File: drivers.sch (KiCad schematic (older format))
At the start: 27 parts, among them U1 K, U2 E, U3 F

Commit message: - added supply sch draft
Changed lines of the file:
@@
 $Descr A4 11693 8268
 encoding utf-8
-Sheet 9 8
+Sheet 8 9
 Title ""
 Date ""
@@
 $EndComp
 $Comp
-L power:GND #PWR?
-U 1 1 5F61F5A5
-P 5200 2000
-F 0 "#PWR?" H 5200 1840 50  0001 C CNN
-F 1 "GND" V 5200 1923 39  0000 R CNN
-F 2 "" H 5200 2000 50  0001 C CNN
-F 3 "" H 5200 2000 50  0001 C CNN
-	1    5200 2000
-	1    0    0    -1
-$EndComp
-$Comp
 L power:+12V #PWR?
 U 1 1 5F61F5AB
@@
 Wire Wire Line
 	5200 2000 5200 1850
-Connection ~ 5200 2000
 Wire Wire Line
 	4950 1700 4600 1700
@@
 $EndComp
 $Comp
-L power:GND #PWR?
-U 1 1 5F61F5ED
-P 6450 1650
-F 0 "#PWR?" H 6450 1490 50  0001 C CNN
-F 1 "GND" V 6450 1573 39  0000 R CNN
-F 2 "" H 6450 1650 50  0001 C CNN
-F 3 "" H 6450 1650 50  0001 C CNN
-	1    6450 1650
-	1    0    0    -1
-$EndComp
-$Comp
 L power:+15V #PWR?
 U 1 1 5F61F5F3
@@
 	4600 1700 4000 1700
 $Comp
-L power:GND #PWR?
-U 1 1 5F620EBC
-P 5200 3600
-F 0 "#PWR?" H 5200 3440 50  0001 C CNN
-F 1 "GND" V 5200 3523 39  0000 R CNN
-F 2 "" H 5200 3600 50  0001 C CNN
-F 3 "" H 5200 3600 50  0001 C CNN
-	1    5200 3600
-	1    0    0    -1
-$EndComp
-$Comp
 L power:+12V #PWR?
 U 1 1 5F620EC2
@@
 Wire Wire Line
 	5200 3600 5200 3450
-Connection ~ 5200 3600
 Wire Wire Line
 	4950 3300 4600 3300
@@
 	4600 3300 4000 3300
 $Comp
-L power:GND #PWR?
-U 1 1 5F62129D
-P 5200 5200
-F 0 "#PWR?" H 5200 5040 50  0001 C CNN
-F 1 "GND" V 5200 5123 39  0000 R CNN
-F 2 "" H 5200 5200 50  0001 C CNN
-F 3 "" H 5200 5200 50  0001 C CNN
-	1    5200 5200
-	1    0    0    -1
-$EndComp
-$Comp
 L power:+12V #PWR?
 U 1 1 5F6212A3
@@
 Wire Wire Line
 	5200 5200 5200 5050
-Connection ~ 5200 5200
 Wire Wire Line
 	4950 4900 4600 4900
@@
 $EndComp
 $Comp
-L power:GND #PWR?
-U 1 1 5F622691
-P 6450 3300
-F 0 "#PWR?" H 6450 3140 50  0001 C CNN
-F 1 "GND" V 6450 3223 39  0000 R CNN
-F 2 "" H 6450 3300 50  0001 C CNN
-F 3 "" H 6450 3300 50  0001 C CNN
-	1    6450 3300
-	1    0    0    -1
-$EndComp
-$Comp
 L power:+15V #PWR?
 U 1 1 5F622697
@@
 $EndComp
 $Comp
-L power:GND #PWR?
-U 1 1 5F622A77
-P 6450 4950
-F 0 "#PWR?" H 6450 4790 50  0001 C CNN
-F 1 "GND" V 6450 4873 39  0000 R CNN
-F 2 "" H 6450 4950 50  0001 C CNN
-F 3 "" H 6450 4950 50  0001 C CNN
-	1    6450 4950
-	1    0    0    -1
-$EndComp
-$Comp
 L power:+15V #PWR?
 U 1 1 5F622A7D
@@
 	1    0    0    -1
 $EndComp
+$Comp
+L power:GND #PWR?
+U 1 1 5F62755D
+P 6450 1650
+AR Path="/5F40DCB9/5F62755D" Ref="#PWR?"  Part="1"
+AR Path="/5F618AB9/5F62755D" Ref="#PWR?"  Part="1"
+AR Path="/5F62755D" Ref="#PWR?"  Part="1"
+AR Path="/5F61C123/5F62755D" Ref="#PWR?"  Part="1"
+F 0 "#PWR?" H 6450 1490 50  0001 C CNN
+F 1 "GND" H 6450 1550 39  0000 C TNN
+F 2 "" H 6450 1650 50  0001 C CNN
+F 3 "" H 6450 1650 50  0001 C CNN
+	1    6450 1650
+	1    0    0    -1
+$EndComp
+$Comp
+L power:GND #PWR?
+U 1 1 5F6278F0
+P 5200 2000
+AR Path="/5F40DCB9/5F6278F0" Ref="#PWR?"  Part="1"
+AR Path="/5F618AB9/5F6278F0" Ref="#PWR?"  Part="1"
+AR Path="/5F6278F0" Ref="#PWR?"  Part="1"
+AR Path="/5F61C123/5F6278F0" Ref="#PWR?"  Part="1"
+F 0 "#PWR?" H 5200 1840 50  0001 C CNN
+F 1 "GND" H 5200 1900 39  0000 C TNN
+F 2 "" H 5200 2000 50  0001 C CNN
+F 3 "" H 5200 2000 50  0001 C CNN
+	1    5200 2000
+	1    0    0    -1
+$EndComp
+$Comp
+L power:GND #PWR?
+U 1 1 5F627D40
+P 6450 3300
+AR Path="/5F40DCB9/5F627D40" Ref="#PWR?"  Part="1"
+AR Path="/5F618AB9/5F627D40" Ref="#PWR?"  Part="1"
+AR Path="/5F627D40" Ref="#PWR?"  Part="1"
+AR Path="/5F61C123/5F627D40" Ref="#PWR?"  Part="1"
+F 0 "#PWR?" H 6450 3140 50  0001 C CNN
+F 1 "GND" H 6450 3200 39  0000 C TNN
+F 2 "" H 6450 3300 50  0001 C CNN
+F 3 "" H 6450 3300 50  0001 C CNN
+	1    6450 3300
+	1    0    0    -1
+$EndComp
+$Comp
+L power:GND #PWR?
+U 1 1 5F6280D3
+P 5200 3600
+AR Path="/5F40DCB9/5F6280D3" Ref="#PWR?"  Part="1"
+AR Path="/5F618AB9/5F6280D3" Ref="#PWR?"  Part="1"
+AR Path="/5F6280D3" Ref="#PWR?"  Part="1"
+AR Path="/5F61C123/5F6280D3" Ref="#PWR?"  Part="1"
+F 0 "#PWR?" H 5200 3440 50  0001 C CNN
+F 1 "GND" H 5200 3500 39  0000 C TNN
+F 2 "" H 5200 3600 50  0001 C CNN
+F 3 "" H 5200 3600 50  0001 C CNN
+	1    5200 3600
+	1    0    0    -1
+$EndComp
+$Comp
+L power:GND #PWR?
+U 1 1 5F628523
+P 6450 4950
+AR Path="/5F40DCB9/5F628523" Ref="#PWR?"  Part="1"
+AR Path="/5F618AB9/5F628523" Ref="#PWR?"  Part="1"
+AR Path="/5F628523" Ref="#PWR?"  Part="1"
+AR Path="/5F61C123/5F628523" Ref="#PWR?"  Part="1"
+F 0 "#PWR?" H 6450 4790 50  0001 C CNN
+F 1 "GND" H 6450 4850 39  0000 C TNN
+F 2 "" H 6450 4950 50  0001 C CNN
+F 3 "" H 6450 4950 50  0001 C CNN
+	1    6450 4950
+	1    0    0    -1
+$EndComp
+$Comp
+L power:GND #PWR?
+U 1 1 5F6288B6
+P 5200 5200
+AR Path="/5F40DCB9/5F6288B6" Ref="#PWR?"  Part="1"
+AR Path="/5F618AB9/5F6288B6" Ref="#PWR?"  Part="1"
+AR Path="/5F6288B6" Ref="#PWR?"  Part="1"
+AR Path="/5F61C123/5F6288B6" Ref="#PWR?"  Part="1"
+F 0 "#PWR?" H 5200 5040 50  0001 C CNN
+F 1 "GND" H 5200 5100 39  0000 C TNN
+F 2 "" H 5200 5200 50  0001 C CNN
+F 3 "" H 5200 5200 50  0001 C CNN
+	1    5200 5200
+	1    0    0    -1
+$EndComp
+Connection ~ 5200 5200
+Connection ~ 5200 3600
+Connection ~ 5200 2000
 $EndSCHEMATC

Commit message: - added footprint & 3D model of DC/DC HV converter - updated battery (to 2x battery holder) - some changes in supply
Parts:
- U1, U2, U3: footprint (none) -> Library_uScope:APD_P2_single
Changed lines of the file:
@@
 $Descr A4 11693 8268
 encoding utf-8
-Sheet 8 9
+Sheet 6 9
 Title ""
 Date ""
@@
 F 0 "U1" H 5728 1751 50  0000 L CNN
 F 1 "K" H 5728 1660 50  0000 L CNN
-F 2 "" H 5500 1700 50  0001 C CNN
+F 2 "Library_uScope:APD_P2_single" H 5500 1700 50  0001 C CNN
 F 3 "" H 5500 1700 50  0001 C CNN
 	1    5500 1700
@@
 F 0 "U2" H 5728 3351 50  0000 L CNN
 F 1 "E" H 5728 3260 50  0000 L CNN
-F 2 "" H 5500 3300 50  0001 C CNN
+F 2 "Library_uScope:APD_P2_single" H 5500 3300 50  0001 C CNN
 F 3 "" H 5500 3300 50  0001 C CNN
 	1    5500 3300
@@
 F 0 "U3" H 5728 4951 50  0000 L CNN
 F 1 "F" H 5728 4860 50  0000 L CNN
-F 2 "" H 5500 4900 50  0001 C CNN
+F 2 "Library_uScope:APD_P2_single" H 5500 4900 50  0001 C CNN
 F 3 "" H 5500 4900 50  0001 C CNN
 	1    5500 4900

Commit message: - W.i.P.
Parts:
- removed C? (x2): 1n, symbol Device:C_Small
- removed Q? (x2): NMOS, symbol Device:Q_NMOS_GDS
- removed R? (x2): 10k, symbol Device:R
- removed R? (x2): 1k, symbol Device:R
- removed R? (x2): 12k, symbol Device:R
- removed R? (x2): 4k3, symbol Device:R
- removed U? (x6): LMC6482, symbol Amplifier_Operational:LMC6482
- added C? (x3): 100n, Capacitor_SMD:C_0805_2012Metric_Pad1.15x1.40mm_HandSolder, symbol Device:C_Small
- added C? (x2): 100p, Capacitor_SMD:C_0805_2012Metric_Pad1.15x1.40mm_HandSolder, symbol Device:C_Small
- added Q? (x2): BUK98150-55A, Package_TO_SOT_SMD:SOT-223-3_TabPin2, symbol Device:Q_NMOS_GDS
- added R? (x2): 10k, Resistor_SMD:R_0603_1608Metric_Pad1.05x0.95mm_HandSolder, symbol Device:R_Small
- added R? (x2): 1k, Resistor_SMD:R_0603_1608Metric_Pad1.05x0.95mm_HandSolder, symbol Device:R_Small
- added R? (x2): 12k, Resistor_SMD:R_0603_1608Metric_Pad1.05x0.95mm_HandSolder, symbol Device:R_Small
- added R? (x2): 4k3, Resistor_SMD:R_0603_1608Metric_Pad1.05x0.95mm_HandSolder, symbol Device:R_Small
- added U? (x3): LM321, Package_TO_SOT_SMD:SOT-23-5, symbol Amplifier_Operational:LM321
- C?: value 1n -> 100p; footprint (none) -> Capacitor_SMD:C_0805_2012Metric_Pad1.15x1.40mm_HandSolder
- Q?: value NMOS -> BUK98150-55A; footprint (none) -> Package_TO_SOT_SMD:SOT-223-3_TabPin2; Mfr. (none) -> Nexperia; Price [PLN] (none) -> 1.60
- R? (x4): footprint (none) -> Resistor_SMD:R_0603_1608Metric_Pad1.05x0.95mm_HandSolder; symbol Device:R -> Device:R_Small
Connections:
- net +12V: now also Q?.2 (D), Q?.2 (D)
- net +15V: now also C?.2, C?.2, C?.2, U?.5 (V+), U?.5 (V+), U?.5 (V+)
- net GND: now also C?.1, C?.1, C?.1, R?.2, R?.2, U?.2 (V-), U?.2 (V-), U?.2 (V-)
- net dac_E: now also R?.1
- net dac_F: now also R?.1
- net at U2.1 (in+): now also Q?.3 (S), R?.1
- net at U3.1 (in+): now also Q?.3 (S), R?.1
- net at C?.1, R?.1: now also U?.4
- net at C?.2, R?.1, R?.2: now also U?.3 (-)
- net at R?.2: now also U?.1 (+)
- new net: R?.2, U?.1 (+) (x2)
- new net: C?.1, R?.1, U?.4 (x2)
- new net: Q?.1 (G), R?.2 (x2)
- new net: C?.2, R?.1, R?.2, U?.3 (-) (x2)
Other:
- moved on the sheet: C?, Q?, R?, U1A, U2A, U3A

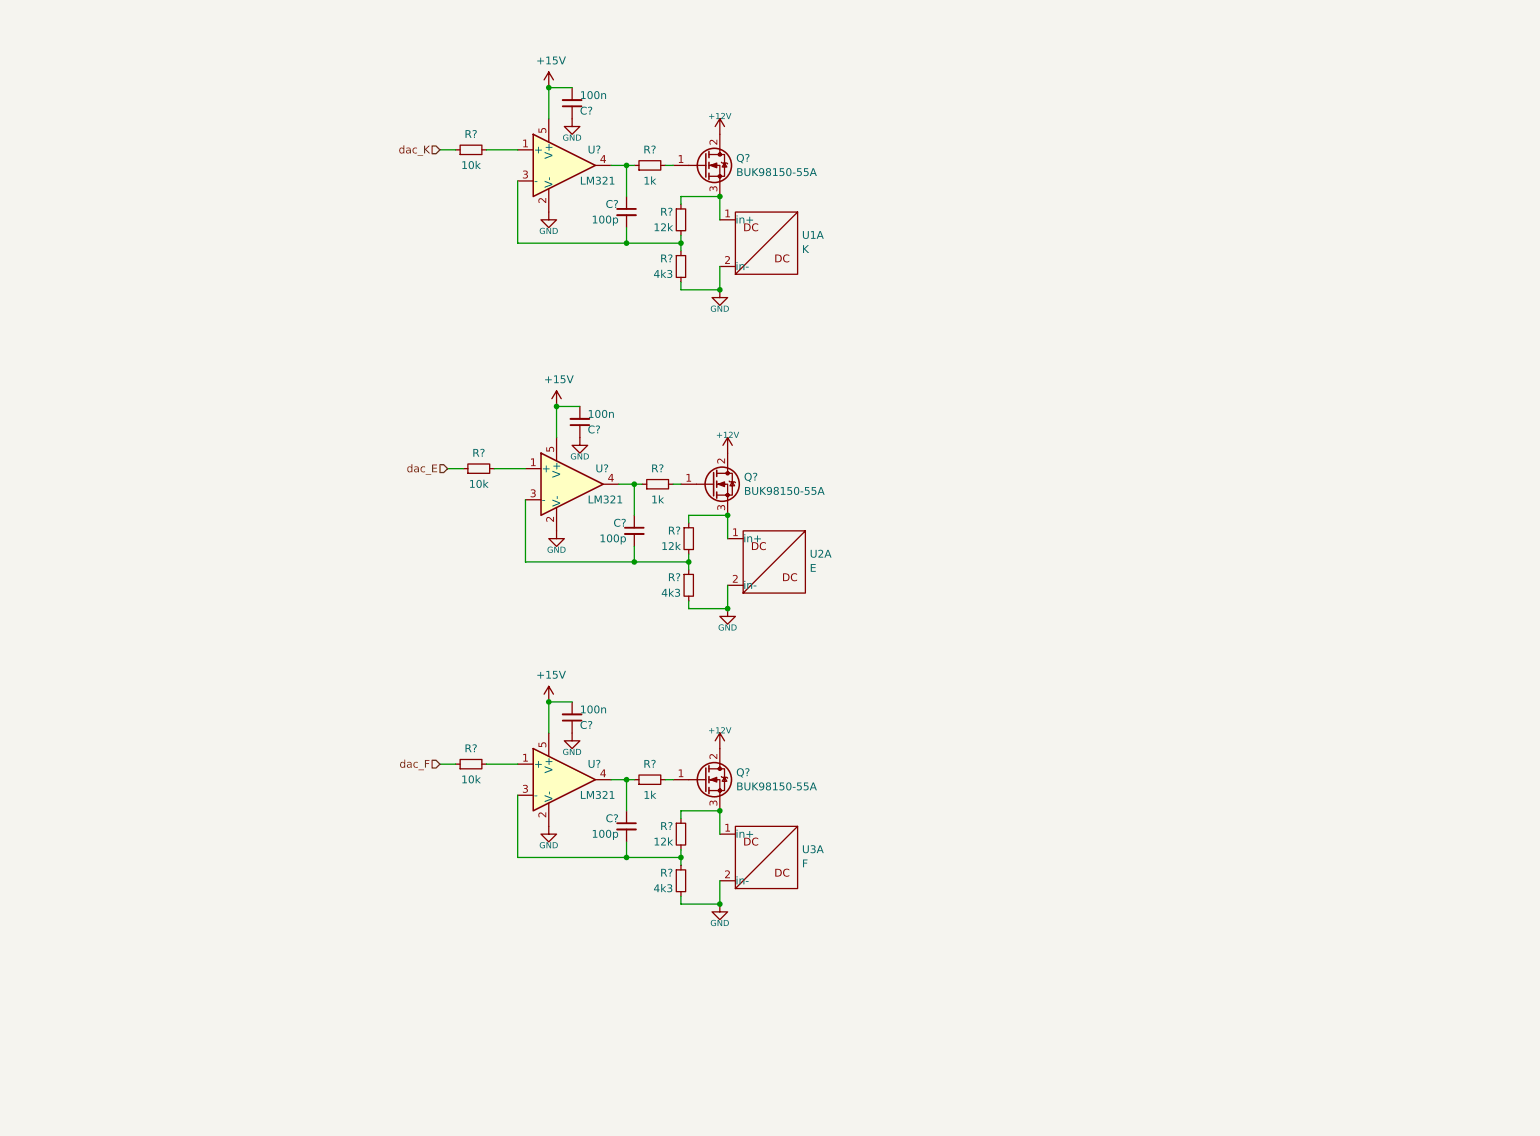
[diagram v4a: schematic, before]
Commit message: - drivers modified - MCU replaced
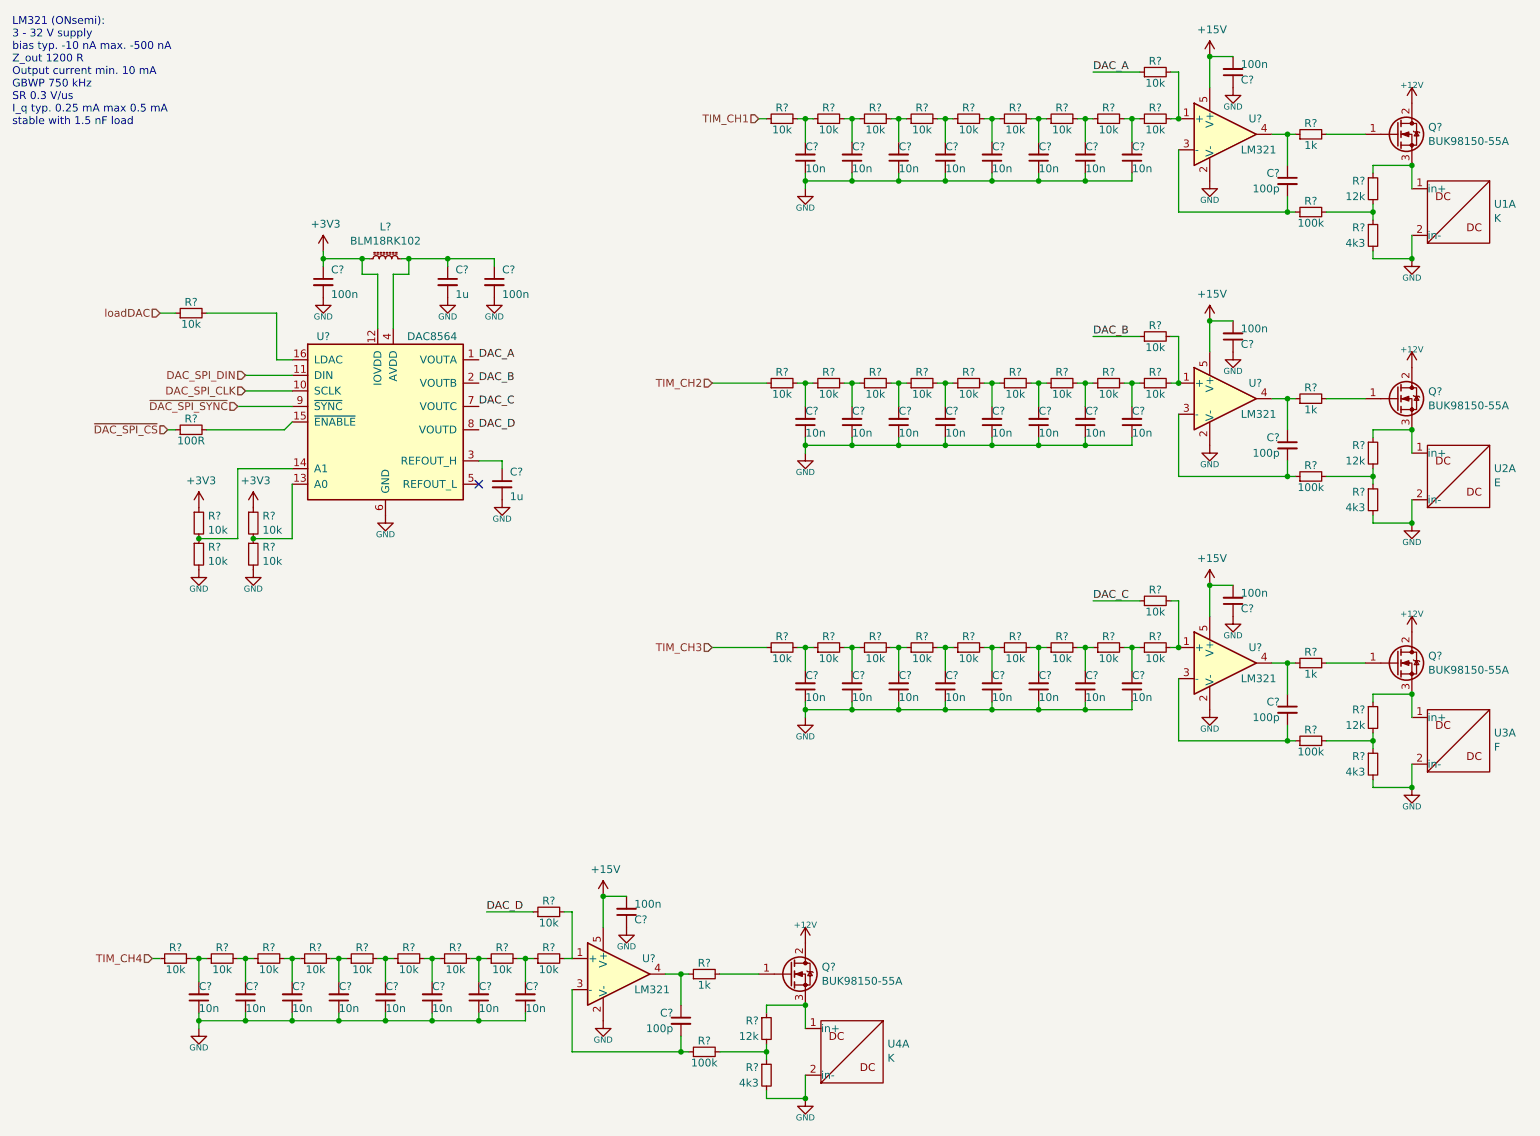
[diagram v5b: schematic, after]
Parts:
- removed R? (x3): 10k, Resistor_SMD:R_0603_1608Metric_Pad1.05x0.95mm_HandSolder, symbol Device:R_Small
- removed R? (x2): 1k, Resistor_SMD:R_0603_1608Metric_Pad1.05x0.95mm_HandSolder, symbol Device:R_Small
- added C? (x32): 10n, Capacitor_SMD:C_0603_1608Metric_Pad1.05x0.95mm_HandSolder, symbol Device:C_Small
- added C?: 100p, Capacitor_SMD:C_0805_2012Metric_Pad1.15x1.40mm_HandSolder, symbol Device:C_Small
- added C?: 100n, Capacitor_SMD:C_0805_2012Metric_Pad1.15x1.40mm_HandSolder, symbol Device:C_Small
- added C? (x2): 100n, Capacitor_SMD:C_0603_1608Metric_Pad1.05x0.95mm_HandSolder, symbol Device:C_Small
- added C? (x2): 1u, Capacitor_SMD:C_0603_1608Metric_Pad1.05x0.95mm_HandSolder, symbol Device:C_Small
- added L?: BLM18RK102, symbol Device:L_Core_Ferrite_Small
- added Q?: BUK98150-55A, Package_TO_SOT_SMD:SOT-223-3_TabPin2, symbol Device:Q_NMOS_GDS
- added R?: 12k, Resistor_SMD:R_0603_1608Metric_Pad1.05x0.95mm_HandSolder, symbol Device:R_Small
- added R?: 4k3, Resistor_SMD:R_0603_1608Metric_Pad1.05x0.95mm_HandSolder, symbol Device:R_Small
- added R? (x45): 10k, Resistor_SMD:R_0603_1608Metric_Pad1.05x0.95mm_HandSolder, symbol Device:R_Small
- added R? (x4): 100k, Resistor_SMD:R_0603_1608Metric_Pad1.05x0.95mm_HandSolder, symbol Device:R_Small
- added R? (x3): 1k, Resistor_SMD:R_0603_1608Metric_Pad1.05x0.95mm_HandSolder, symbol Device:R_Small
- added R?: 100R, Resistor_SMD:R_0603_1608Metric_Pad1.05x0.95mm_HandSolder, symbol Device:R_Small
- added U4: K, Library_uScope:APD_P2_single, symbol uScope:APD_P2_single
- added U?: LM321, Package_TO_SOT_SMD:SOT-23-5, symbol Amplifier_Operational:LM321
- added U?: DAC8564, symbol miscellaneous:DAC8564
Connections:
- net +12V: now also Q?.2 (D)
- net +15V: now also C?.2, U?.5 (V+)
- net GND: now also C?.1, C?.1, C?.1, C?.1, C?.1, C?.1, C?.1, C?.1, C?.1, C?.1, C?.1, C?.1, C?.1, C?.1, C?.1, C?.1, C?.1, C?.1, C?.1, C?.1, C?.1, C?.1, C?.1, C?.1, C?.1, C?.1, C?.1, C?.1, C?.1, C?.1, C?.1, C?.1, C?.1, C?.2, C?.2, C?.2, C?.2, R?.2, R?.2, R?.2, U4.2 (in-), U?.2 (V-), U?.6 (GND)
- net at U?.1 (+): now also R?.2, R?.2 (x3)
- net at R?.1, R?.2: now also R?.2; no longer C?.2, U?.3 (-) (x3)
- net at C?.1, U?.4: now also R?.1 (x2)
- net at Q?.1 (G): now also R?.2 (x2)
- new net: C?.2, R?.1, U?.3 (-) (x4)
- new net: C?.2, R?.1, R?.2 (x32)
- new net: Q?.3 (S), R?.1, U4.1 (in+)
- new net: R?.1, R?.2, R?.2
- new net: Q?.1 (G), R?.2
- new net: C?.1, R?.1, U?.4
- new net: R?.2, R?.2, U?.1 (+)
- new net: R?.1, R?.2, U?.14 (A1)
- new net: R?.1, R?.2, U?.13 (A0)
- new net: R?.2, U?.15 (~ENABLE)
- new net: R?.2, U?.16 (LDAC)
- new net: C?.1, U?.3 (REFOUT_H)
- new net: C?.1, C?.1, L?.2, U?.4 (AVDD)
- new net +3V3: C?.1, L?.1, R?.1, R?.1, U?.12 (IOVDD)
- new net DAC_A: R?.1, U?.1 (VOUTA)
- new net DAC_B: R?.1, U?.2 (VOUTB)
- new net DAC_C: R?.1, U?.7 (VOUTC)
- new net DAC_D: R?.1, U?.8 (VOUTD)
- new net DAC_SPI_CLK: U?.10 (SCLK)
- new net DAC_SPI_DIN: U?.11 (DIN)
- new net TIM_CH1: R?.1
- new net TIM_CH2: R?.1
- new net TIM_CH3: R?.1
- new net TIM_CH4: R?.1
- new net loadDAC: R?.1
- new net ~DAC_SPI_CS: R?.1
- new net ~DAC_SPI_SYNC: U?.9 (~SYNC)
- no-connect marks 0 -> 1
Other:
- note added: "LM321 (ONsemi):\n3 - 32 V supply\nbias typ. -10 nA max. -500 nA\nZ_out 1200 R\nOutput current min. 10 mA\nGBWP 750 kHz\nSR 0.3 V/us\nI_q typ. 0.25 mA max 0.5 mA\nstable with 1.5 nF load\n"
- moved on the sheet: C?, Q?, R?, U1A, U2A, U3A, U?
